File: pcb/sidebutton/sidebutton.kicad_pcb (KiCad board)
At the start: 2 copper layers, 32 x 19.5 mm, 7 parts, among them J1 Conn_01x04, SW1 SW_DIP_x01

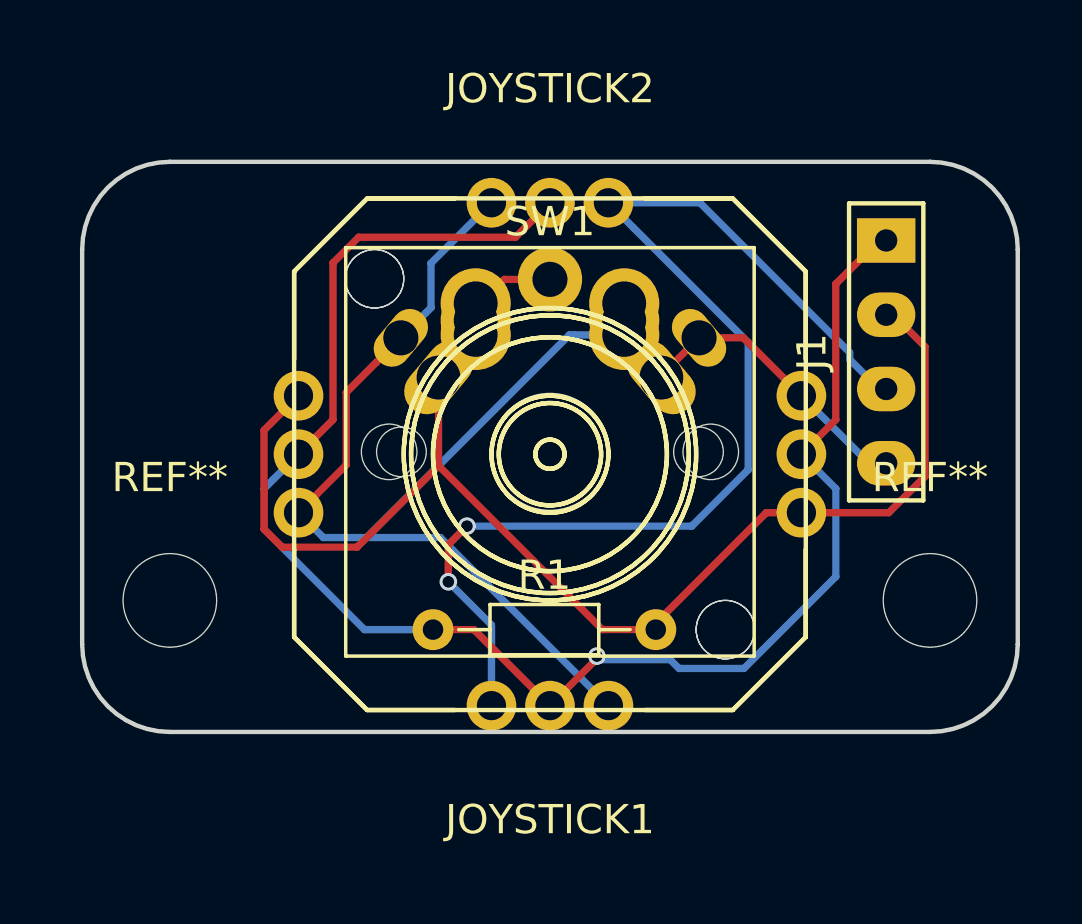
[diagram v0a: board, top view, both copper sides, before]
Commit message: sidebutton: add GND solid
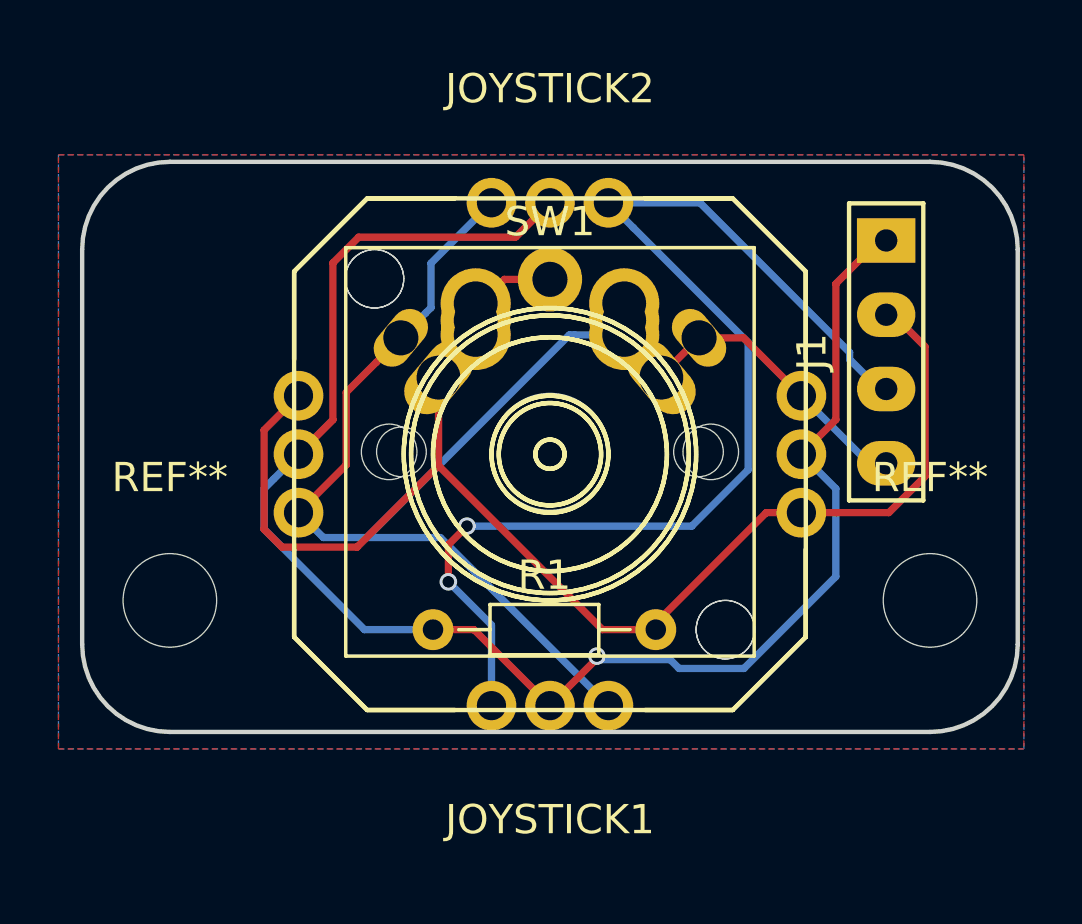
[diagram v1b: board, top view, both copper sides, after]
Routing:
- added copper zone on B.Cu, net GND
- added copper zone on F.Cu, net GND
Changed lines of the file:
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@@
     (links 25)
     (no_connects 0)
-    (area -3.075001 -15.075001 29.075001 4.575001)
+    (area -9.560143 -18.478 35.560143 8.578)
     (thickness 1.6)
     (drawings 8)
@@
   (segment (start 6.031012 -4.631012) (end 6.031012 -7.111012) (width 0.25) (layer F.Cu) (net 4))
   (segment (start 7.054433 -8.134433) (end 7.9 -8.98) (width 0.25) (layer F.Cu) (net 4))
+  (zone (net 4) (net_name GND) (layer F.Cu) (hatch edge 0.508)
+    (connect_pads (clearance 0.508))
+    (min_thickness 0.254)
+    (fill yes (arc_segments 16) (thermal_gap 0.508) (thermal_bridge_width 0.508))
+    (polygon
+      (pts
+        (xy 29.21 -15.24) (xy 29.21 5.08) (xy -3.81 5.08) (xy -3.81 -15.24)
+      )
+    )
+  )
+  (zone (net 4) (net_name GND) (layer B.Cu) (hatch edge 0.508)
+    (connect_pads (clearance 0.508))
+    (min_thickness 0.254)
+    (fill yes (arc_segments 16) (thermal_gap 0.508) (thermal_bridge_width 0.508))
+    (polygon
+      (pts
+        (xy 29.21 -15.24) (xy -3.81 -15.24) (xy -3.81 5.08) (xy 29.21 5.08)
+      )
+    )
+  )
 )

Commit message: fix sidebutton mounting position
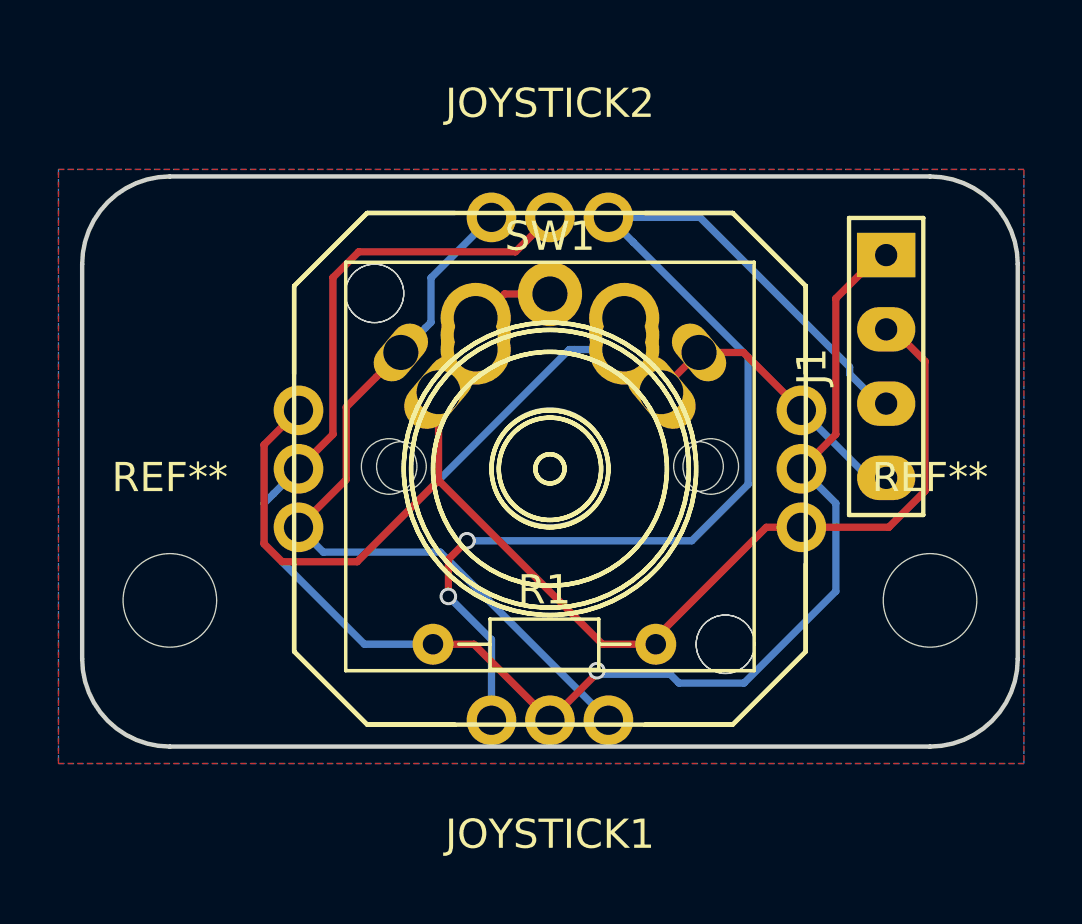
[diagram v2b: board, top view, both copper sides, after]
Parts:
- moved J1 0.50 mm to (24.5, -8.00)
- moved JOYSTICK1 0.50 mm to (13.0, -4.50)
- moved JOYSTICK2 0.50 mm to (13.0, -4.50)
- moved R1 0.50 mm to (9.00, 1.50)
- moved SW1 0.50 mm to (13.0, -4.58)
